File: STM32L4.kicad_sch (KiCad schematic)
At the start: 32 parts, among them J1 Conn_01x04_Pin, U10 STM32L476RGTx, U11 TCAN334, U12 MR20H40, Y2 8 MHZ Oscillator

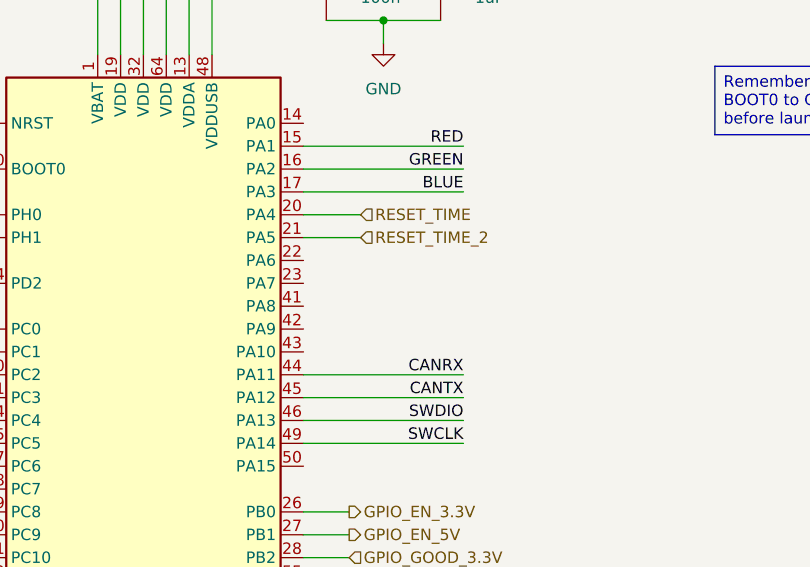
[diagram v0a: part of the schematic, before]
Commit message: added current sensing and e-fuses
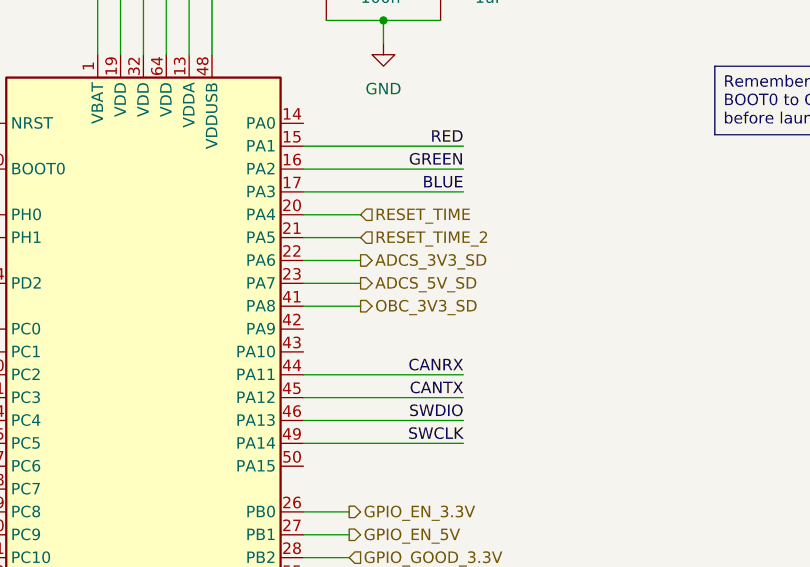
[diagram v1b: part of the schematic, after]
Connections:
- net ADCS_3V3_SD: now reaches U10.22 (PA6)
- net ADCS_5V_SD: now reaches U10.23 (PA7)
- net OBC_3V3_SD: now reaches U10.41 (PA8)
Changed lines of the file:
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@@
+	(wire
+		(pts
+			(xy 166.37 77.47) (xy 160.02 77.47)
+		)
+		(stroke
+			(width 0)
+			(type default)
+		)
+	)
 	(wire
 		(pts
@@
 	(wire
 		(pts
+			(xy 160.02 82.55) (xy 166.37 82.55)
+		)
+		(stroke
+			(width 0)
+			(type default)
+		)
+	)
+	(wire
+		(pts
 			(xy 252.73 149.86) (xy 252.73 152.4)
 		)
@@
 		(pts
 			(xy 156.21 33.02) (xy 156.21 41.91)
+		)
+		(stroke
+			(width 0)
+			(type default)
+		)
+	)
+	(wire
+		(pts
+			(xy 160.02 80.01) (xy 166.37 80.01)
 		)
 		(stroke
@@
 			)
 			(justify right bottom)
+		)
+	)
+	(hierarchical_label "OBC_3V3_SD"
+		(shape output)
+		(at 166.37 82.55 0)
+		(effects
+			(font
+				(size 1.27 1.27)
+			)
+			(justify left)
 		)
 	)
@@
 		)
 	)
+	(hierarchical_label "ADCS_3V3_SD"
+		(shape output)
+		(at 166.37 77.47 0)
+		(effects
+			(font
+				(size 1.27 1.27)
+			)
+			(justify left)
+		)
+	)
 	(hierarchical_label "RESET_TIME"
 		(shape input)
@@
 		)
 	)
+	(hierarchical_label "ADCS_5V_SD"
+		(shape output)
+		(at 166.37 80.01 0)
+		(effects
+			(font
+				(size 1.27 1.27)
+			)
+			(justify left)
+		)
+	)

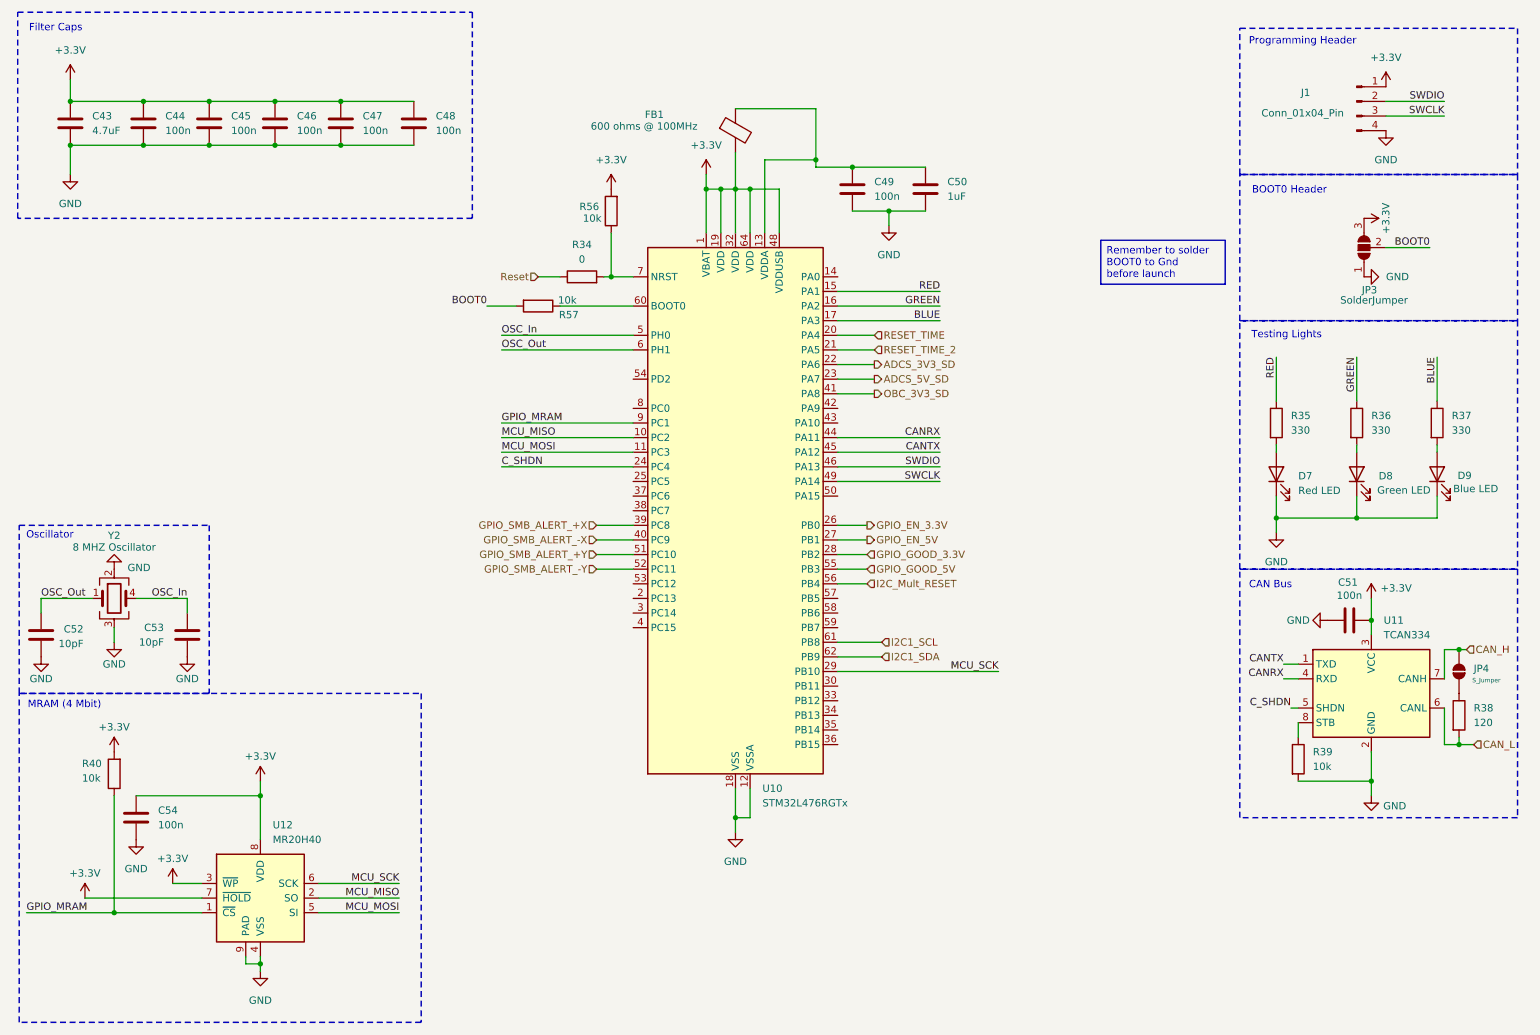
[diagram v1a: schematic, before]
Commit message: Added connectors to schematic
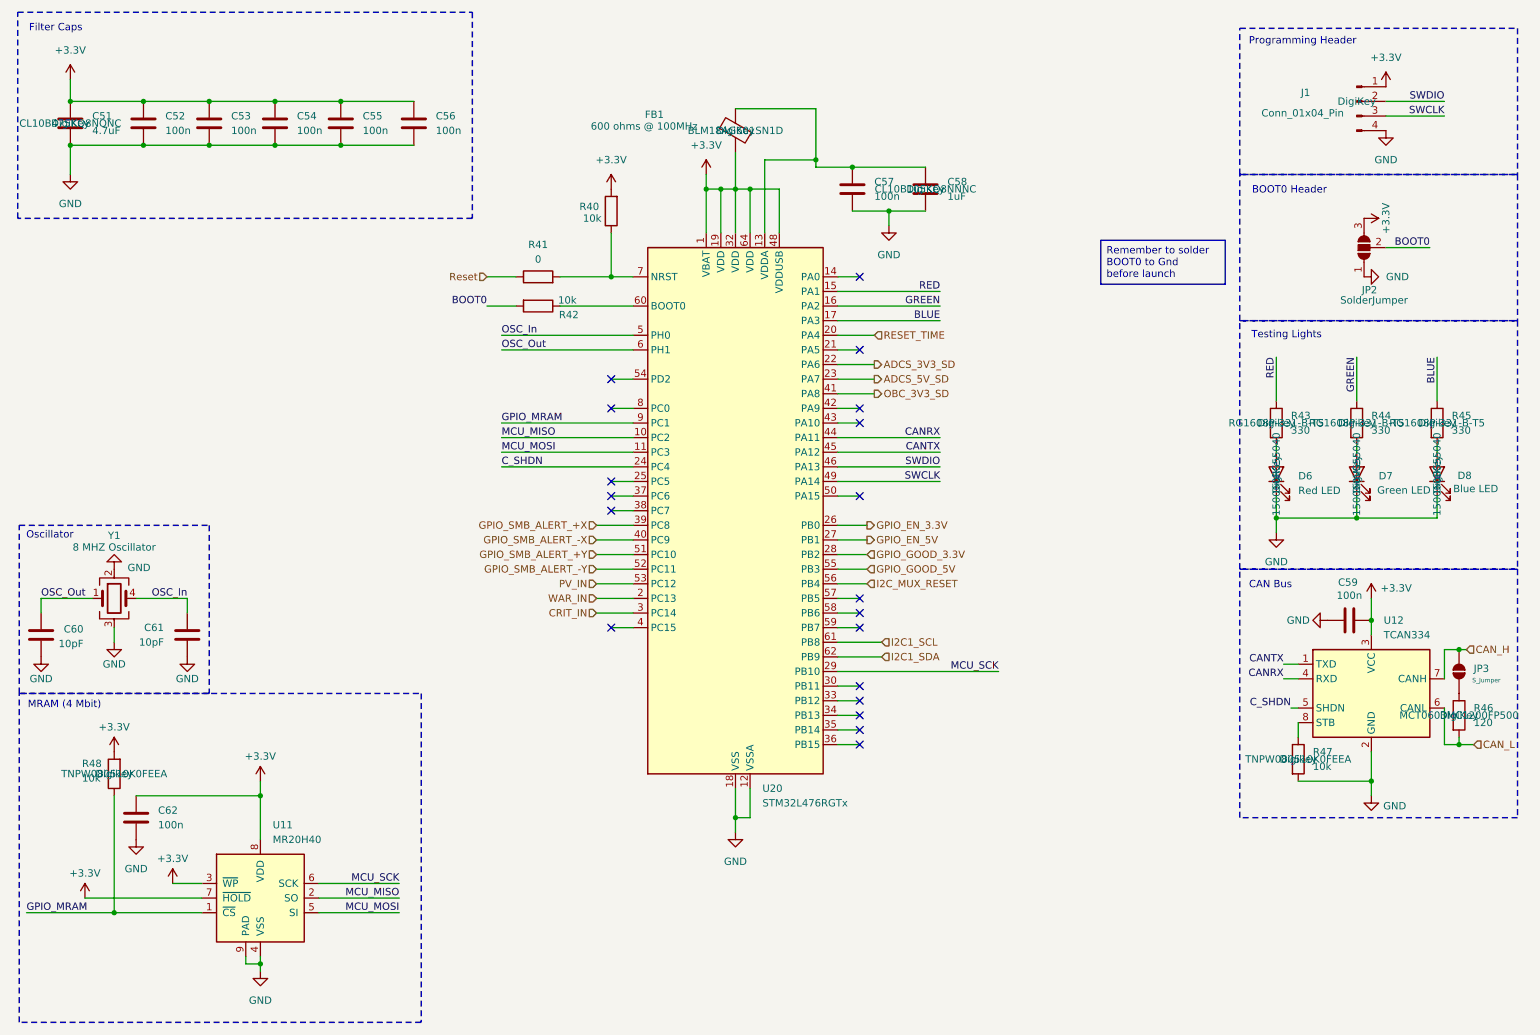
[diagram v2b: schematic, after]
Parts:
- removed U10: STM32L476RGTx, LTC4162IUFD-LADM_PBF:QFN50P500X400X80-29N, symbol MCU_ST_STM32L4:STM32L476RGTx
- removed U12: MR20H40, DBV5, symbol Memory_NVRAM:MR20H40
- added U11: MR20H40, Package_DFN_QFN:DFN-8-1EP_6x5mm_P1.27mm_EP4x4mm, symbol Memory_NVRAM:MR20H40
- added U20: STM32L476RGTx, Package_QFP:LQFP-64_10x10mm_P0.5mm, symbol MCU_ST_STM32L4:STM32L476RGTx
- C51: renamed from C43; footprint Capacitor_SMD:C_0805_2012Metric -> Capacitor_SMD:C_0603_1608Metric; MANUFACTURER (none) -> DigiKey; MANUFACTURER_PART_NUMBER (none) -> CL10B475KQ8NQNC
- C58: renamed from C50; MANUFACTURER (none) -> DigiKey; MANUFACTURER_PART_NUMBER (none) -> CL10B105KQ8NNNC
- C60: renamed from C52; footprint Capacitor_SMD:C_01005_0402Metric -> Capacitor_SMD:C_0603_1608Metric; MANUFACTURER_PART_NUMBER GRM1555C1H100FA01D -> 06035C100K4T4A
- C61: renamed from C53; footprint Capacitor_SMD:C_01005_0402Metric -> Capacitor_SMD:C_0603_1608Metric; MANUFACTURER_PART_NUMBER GRM1555C1H100FA01D -> 06035C100K4T4A
- D6: renamed from D7; MANUFACTURER (none) -> DigiKey; MANUFACTURER_PART_NUMBER (none) -> 150060RS55040
- D7: renamed from D8; MANUFACTURER (none) -> DigiKey; MANUFACTURER_PART_NUMBER (none) -> 150060VS55040
- D8: renamed from D9; MANUFACTURER (none) -> DigiKey; MANUFACTURER_PART_NUMBER (none) -> 150060BS55040
- FB1: MANUFACTURER (none) -> DigiKey; MANUFACTURER_PART_NUMBER (none) -> BLM18AG601SN1D
- J1: MANUFACTURER (none) -> DigiKey
- R40: renamed from R56; footprint (none) -> Resistor_SMD:R_0805_2012Metric; MANUFACTURER (none) -> Digikey; MANUFACTURER_PART_NUMBER (none) -> TNPW080510K0FEEA
- R41: renamed from R34; footprint (none) -> Resistor_SMD:R_0603_1608Metric; MANUFACTURER (none) -> Digikey; MANUFACTURER_PART_NUMBER (none) -> MCT0603MZ0000ZP500
- R42: renamed from R57; footprint (none) -> Resistor_SMD:R_0805_2012Metric; MANUFACTURER (none) -> Digikey; MANUFACTURER_PART_NUMBER (none) -> TNPW080510K0FEEA
- R43: renamed from R35; MANUFACTURER (none) -> Digikey; MANUFACTURER_PART_NUMBER (none) -> RG1608P-331-B-T5
- R44: renamed from R36; MANUFACTURER (none) -> Digikey; MANUFACTURER_PART_NUMBER (none) -> RG1608P-331-B-T5
- R45: renamed from R37; MANUFACTURER (none) -> Digikey; MANUFACTURER_PART_NUMBER (none) -> RG1608P-331-B-T5
- R46: renamed from R38; footprint (none) -> Resistor_SMD:R_0603_1608Metric; MANUFACTURER (none) -> DigiKey; MANUFACTURER_PART_NUMBER (none) -> MCT0603MC1200FP500
- R47: renamed from R39; footprint (none) -> Resistor_SMD:R_0805_2012Metric; MANUFACTURER (none) -> Digikey; MANUFACTURER_PART_NUMBER (none) -> TNPW080510K0FEEA
- R48: renamed from R40; footprint (none) -> Resistor_SMD:R_0805_2012Metric; MANUFACTURER (none) -> Digikey; MANUFACTURER_PART_NUMBER (none) -> TNPW080510K0FEEA
- U12: renamed from U11; footprint LTC4162IUFD-LADM_PBF:QFN50P500X400X80-29N -> Package_SO:SOIC-8_3.9x4.9mm_P1.27mm
- renumbered C44 to C52, C45 to C53, C46 to C54, C47 to C55, C48 to C56, C49 to C57, C51 to C59, C54 to C62, JP3 to JP2, JP4 to JP3, Y2 to Y1
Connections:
- net +3.3V: now also U11.3 (~{WP}), U11.7 (~{HOLD}), U11.8 (VDD), U20.1 (VBAT), U20.19 (VDD), U20.32 (VDD), U20.48 (VDDUSB), U20.64 (VDD)
- net ADCS_3V3_SD: now also U20.22 (PA6)
- net ADCS_5V_SD: now also U20.23 (PA7)
- net BLUE: now also U20.17 (PA3)
- net CANRX: now also U20.44 (PA11)
- net CANTX: now also U20.45 (PA12)
- net C_SHDN: now also U20.24 (PC4)
- net GND: now also U11.4 (VSS), U11.9 (PAD), U20.12 (VSSA), U20.18 (VSS), U20.31 (VSS), U20.47 (VSS), U20.63 (VSS)
- net GPIO_EN_3.3V: now also U20.26 (PB0)
- net GPIO_EN_5V: now also U20.27 (PB1)
- net GPIO_GOOD_3.3V: now also U20.28 (PB2)
- net GPIO_GOOD_5V: now also U20.55 (PB3)
- net GPIO_MRAM: now also U11.1 (~{CS}), U20.9 (PC1)
- net GPIO_SMB_ALERT_+X: now also U20.39 (PC8)
- net GPIO_SMB_ALERT_+Y: now also U20.51 (PC10)
- net GPIO_SMB_ALERT_-X: now also U20.40 (PC9)
- net GPIO_SMB_ALERT_-Y: now also U20.52 (PC11)
- net GREEN: now also U20.16 (PA2)
- net I2C1_SCL: now also U20.61 (PB8)
- net I2C1_SDA: now also U20.62 (PB9)
- net MCU_MISO: now also U11.2 (SO), U20.10 (PC2)
- net MCU_MOSI: now also U11.5 (SI), U20.11 (PC3)
- net MCU_SCK: now also U11.6 (SCK), U20.29 (PB10)
- net OBC_3V3_SD: now also U20.41 (PA8)
- net OSC_In: now also U20.5 (PH0)
- net OSC_Out: now also U20.6 (PH1)
- net RED: now also U20.15 (PA1)
- net RESET_TIME: now also U20.20 (PA4)
- net SWCLK: now also U20.49 (PA14)
- net SWDIO: now also U20.46 (PA13)
- net at R40.1, R41.2: now also U20.7 (NRST)
- net at C57.1, C58.1, FB1.1: now also U20.13 (VDDA)
- net at R42.1: now also U20.60 (BOOT0)
- new net CRIT_IN: U20.3 (PC14)
- new net I2C_MUX_RESET: U20.56 (PB4)
- new net PV_IN: U20.53 (PC12)
- new net WAR_IN: U20.2 (PC13)
- no-connect marks 0 -> 19
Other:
- moved on the sheet: R41

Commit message: A bunch of misc schematic changes
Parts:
- removed U20: STM32L476RGTx, Package_QFP:LQFP-64_10x10mm_P0.5mm, symbol MCU_ST_STM32L4:STM32L476RGTx
- added C90: 100n, Capacitor_SMD:C_0603_1608Metric, symbol Device:C
- added JP4: S_Jumper, Jumper:SolderJumper-2_P1.3mm_Open_TrianglePad1.0x1.5mm, symbol Jumper:SolderJumper_2_Open
- added R96: 10k, Resistor_SMD:R_0805_2012Metric, symbol Device:R
- added R97: 120, Resistor_SMD:R_0603_1608Metric, symbol Device:R
- added U20: TCAN334GDCNT, Package_TO_SOT_SMD:SOT-23-8, symbol Interface_CAN_LIN:TCAN334
- added U21: STM32L496RGTx, Package_QFP:LQFP-64_10x10mm_P0.5mm, symbol MCU_ST_STM32L4:STM32L496RGTx
- U8: renamed from U12; value TCAN334 -> TCAN334GDCNT; footprint Package_SO:SOIC-8_3.9x4.9mm_P1.27mm -> Package_TO_SOT_SMD:SOT-23-8
- renumbered C51 to C15, C52 to C16, C53 to C17, C54 to C18, C55 to C19, C56 to C20, C57 to C21, C58 to C22, C59 to C23, C60 to C24, C61 to C25, C62 to C26, D6 to D2, D7 to D3, D8 to D4, R40 to R12, R41 to R13, R42 to R14, R43 to R15, R44 to R16, R45 to R17, R46 to R18, R47 to R19, R48 to R20, U11 to U9
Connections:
- net +3.3V: now also C90.2, U20.3 (VCC), U21.1 (VBAT), U21.19 (VDD), U21.32 (VDD), U21.48 (VDDUSB), U21.64 (VDD)
- net ADCS_3V3_SD: now also U21.22 (PA6)
- net ADCS_5V_SD: now also U21.23 (PA7)
- net BLUE: now also U21.17 (PA3)
- net CANRX: now also U21.44 (PA11)
- net CANTX: now also U21.45 (PA12)
- net CRIT_IN: now also U21.3 (PC14)
- net C_SHDN: now also U21.24 (PC4)
- net GND: now also C90.1, R96.2, U20.2 (GND), U21.12 (VSSA), U21.18 (VSS), U21.31 (VSS), U21.47 (VSS), U21.63 (VSS)
- net GPIO_EN_3.3V: now also U21.26 (PB0)
- net GPIO_EN_5V: now also U21.27 (PB1)
- net GPIO_GOOD_3.3V: now also U21.28 (PB2)
- net GPIO_GOOD_5V: now also U21.55 (PB3)
- net GPIO_MRAM: now also U21.9 (PC1)
- net GPIO_SMB_ALERT_+X: now also U21.39 (PC8)
- net GPIO_SMB_ALERT_+Y: now also U21.51 (PC10)
- net GPIO_SMB_ALERT_-X: now also U21.40 (PC9)
- net GPIO_SMB_ALERT_-Y: now also U21.52 (PC11)
- net GREEN: now also U21.16 (PA2)
- net I2C1_SCL: now also U21.61 (PB8)
- net I2C1_SDA: now also U21.62 (PB9)
- net I2C_MUX_RESET: now also U21.56 (PB4)
- net MCU_MISO: now also U21.10 (PC2)
- net MCU_MOSI: now also U21.11 (PC3)
- net MCU_SCK: now also U21.29 (PB10)
- net OBC_3V3_SD: now also U21.41 (PA8)
- net OSC_In: now also U21.5 (PH0)
- net OSC_Out: now also U21.6 (PH1)
- net PV_IN: now also U21.53 (PC12)
- net RED: now also U21.15 (PA1)
- net RESET_TIME: now also U21.20 (PA4)
- net SWCLK: now also U21.49 (PA14)
- net SWDIO: now also U21.46 (PA13)
- net WAR_IN: now also U21.2 (PC13)
- net at R12.1, R13.2: now also U21.7 (NRST)
- net at C21.1, C22.1, FB1.1: now also U21.13 (VDDA)
- net at R14.1: now also U21.60 (PH3)
- new net: JP4.1 (A), R97.1
- new net: R96.1, U20.8 (STB)
- new net CANRX2: U20.4 (RXD), U21.33 (PB12)
- new net CANTX2: U20.1 (TXD), U21.34 (PB13)
- new net CAN_H2: JP4.2 (B), U20.7 (CANH)
- new net CAN_L2: R97.2, U20.6 (CANL)
- new net C_SHDN2: U20.5 (SHDN), U21.25 (PC5)
- new net MPPT_SYNC: U21.21 (PA5)
- no-connect marks 19 -> 15
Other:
- note added: "CAN Bus 1"
- note added: "CAN Bus 2"
- note removed: "CAN Bus"
- moved on the sheet: C21, C22, C23, D2, D3, D4, FB1, J1, JP2, JP3, R12, R13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
